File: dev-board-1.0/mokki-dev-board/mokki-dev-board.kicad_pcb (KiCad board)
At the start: 2 copper layers, 100 x 50 mm, 45 parts, among them J1 USB_B_Micro, J2 SWD connector, J3 OLED_Connector, J4 BLE_Connector, J5 DEBUG_Conn, J6 User port, Q1 BC847B, SW1 SW_PWR, SW10 BTN_B, SW2 BTN_RST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

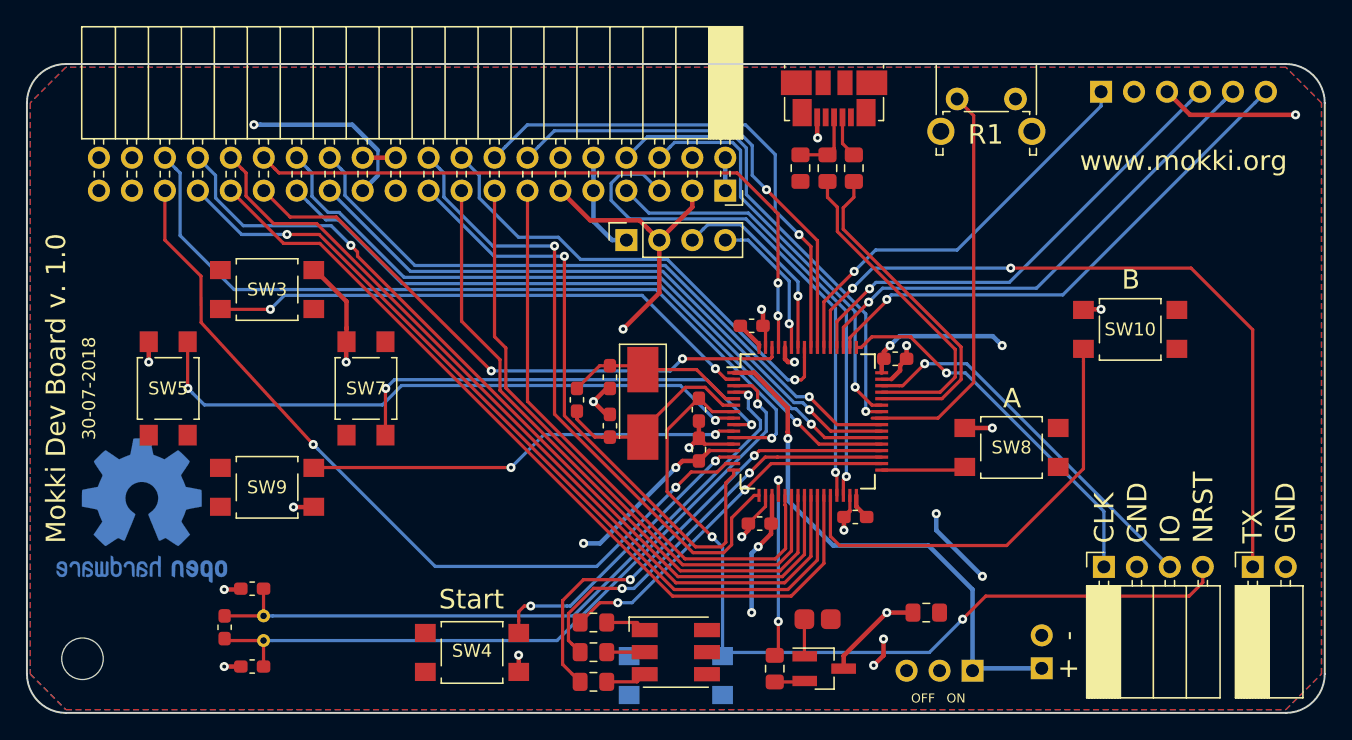
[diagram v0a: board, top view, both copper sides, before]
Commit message: Shrinked from 50mm to 45mm
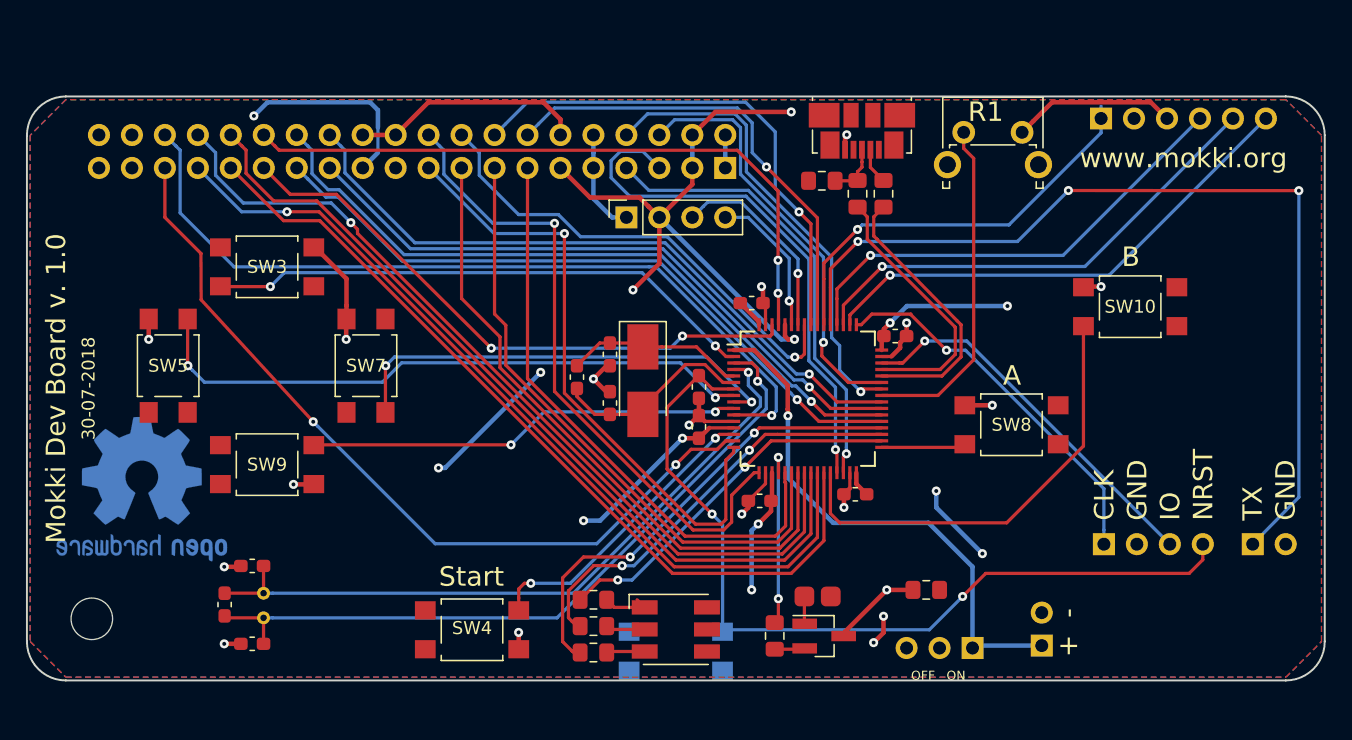
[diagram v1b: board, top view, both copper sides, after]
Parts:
- J2: footprint Connector_PinSocket_2.54mm:PinSocket_1x04_P2.54mm_Horizontal -> Connector_PinSocket_2.54mm:PinSocket_1x04_P2.54mm_Horizontal-no-drawing
- J5: footprint Connector_PinSocket_2.54mm:PinSocket_1x02_P2.54mm_Horizontal -> Connector_PinSocket_2.54mm:PinSocket_1x02_P2.54mm_Horizontal-no-drawing
- J6: footprint Connector_PinSocket_2.54mm:PinSocket_2x20_P2.54mm_Horizontal -> Connector_PinSocket_2.54mm:PinSocket_2x20_P2.54mm_Horizontal-no-drawing
- moved J1 3.30 mm to (162.8, 85.2)
- moved REF** 3.16 mm to (103.5, 122.8)
- moved R9 3.04 mm to (162.5, 90.0)
- moved R8 3.02 mm to (164.5, 90.0)
- moved SW6 2.62 mm to (170.7, 85.3)
- moved R3 2.52 mm to (156.1, 124.1)
- moved Q1 2.51 mm to (159.9, 124.1)
- moved R6 2.26 mm to (142.2, 125.3)
- moved J4 2.06 mm to (181.3, 84.2)
- moved R5 2.00 mm to (142.2, 123.3)
- moved R7 1.92 mm to (159.8, 89.0), turned to 0 degrees
- moved SW2 1.87 mm to (148.5, 125.2)
- moved BT1 1.75 mm to (176.7, 124.8)
- moved C1 1.75 mm to (143.4, 102.4)
- moved C10 1.75 mm to (150.3, 108.0)
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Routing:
- net GND: track 89.7 -> 129.7 mm
- net /USART5_TX: track 57.0 -> 71.6 mm, vias 2 -> 3
- net VCC: track 70.9 -> 83.4 mm, vias 9 -> 11
- net /GPIO_PA8: track 31.3 -> 26.1 mm
- net /USB_DM: track 26.1 -> 21.3 mm
- net /USB_DP: track 25.3 -> 20.6 mm
- net /UART4_TX: track 40.3 -> 37.5 mm
- net /GPIO_PA15: track 40.7 -> 39.1 mm
- net Net-(J1-Pad3): track 5.50 -> 4.24 mm
- net /USART1_RX: track 31.6 -> 32.7 mm
- net /UART4_RX: track 37.3 -> 36.2 mm
- net Net-(D1-Pad1): track 3.17 -> 4.00 mm
- net /DAC: track 14.8 -> 14.0 mm
- net Net-(LS1-Pad2): track 2.87 -> 2.11 mm
- net /USART1_TX: track 35.6 -> 36.2 mm
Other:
- board size 100 x 50 mm -> 100 x 45 mm

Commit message: Revert "Shrinked from 50mm to 45mm"
This reverts commit b318c16d80a30d8fc187a8b3fd500b0e07cadd18.
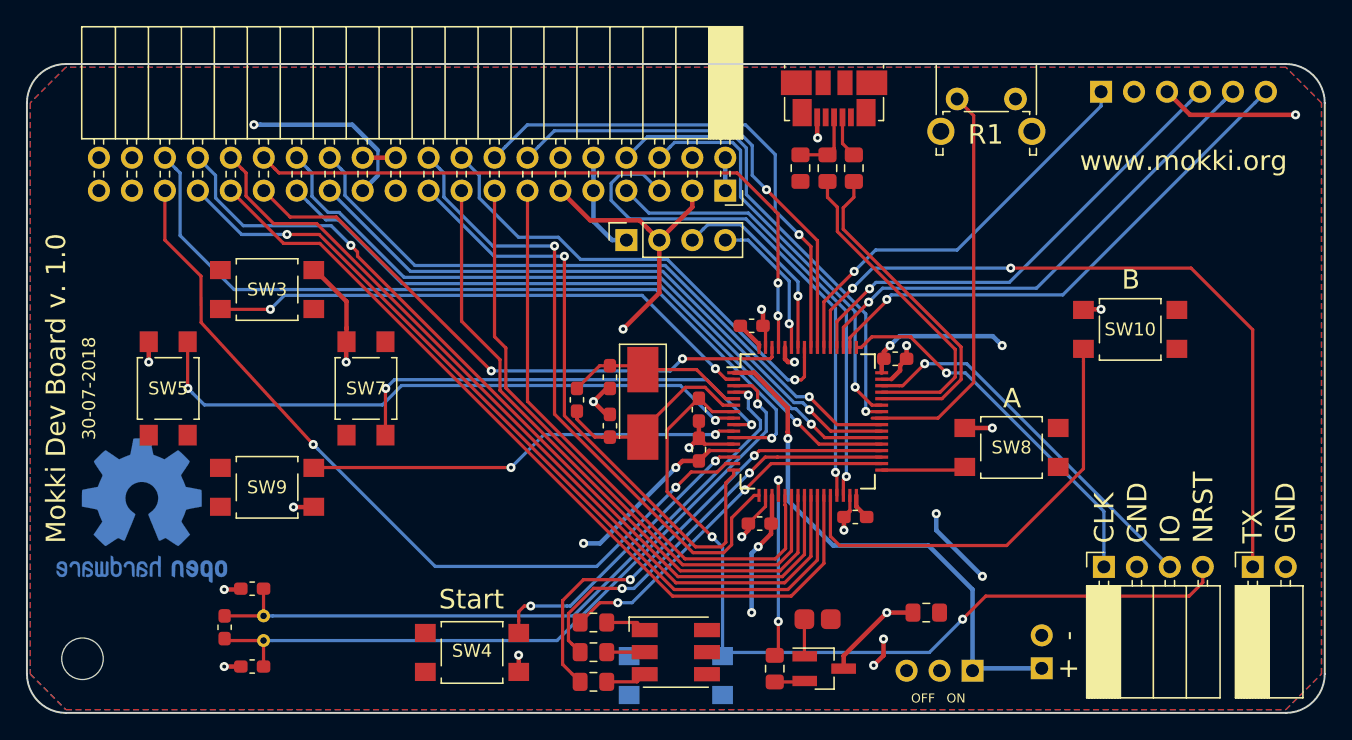
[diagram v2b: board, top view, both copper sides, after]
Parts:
- J2: footprint Connector_PinSocket_2.54mm:PinSocket_1x04_P2.54mm_Horizontal-no-drawing -> Connector_PinSocket_2.54mm:PinSocket_1x04_P2.54mm_Horizontal
- J5: footprint Connector_PinSocket_2.54mm:PinSocket_1x02_P2.54mm_Horizontal-no-drawing -> Connector_PinSocket_2.54mm:PinSocket_1x02_P2.54mm_Horizontal
- J6: footprint Connector_PinSocket_2.54mm:PinSocket_2x20_P2.54mm_Horizontal-no-drawing -> Connector_PinSocket_2.54mm:PinSocket_2x20_P2.54mm_Horizontal
- moved J1 3.30 mm to (160.7, 82.6)
- moved REF** 3.16 mm to (102.8, 125.8)
- moved R9 3.04 mm to (160.2, 88.0)
- moved R8 3.02 mm to (162.2, 88.0)
- moved SW6 2.62 mm to (170.2, 82.7)
- moved R3 2.52 mm to (156.1, 126.6)
- moved Q1 2.51 mm to (159.9, 126.6)
- moved R6 2.26 mm to (142.2, 127.6)
- moved J4 2.06 mm to (181.3, 82.1)
- moved R5 2.00 mm to (142.2, 125.3)
- moved R7 1.92 mm to (158.1, 88.0), turned to 90 degrees
- moved SW2 1.87 mm to (148.5, 127.1)
- moved BT1 1.75 mm to (176.7, 126.6)
- moved C1 1.75 mm to (143.4, 104.1)
- moved C10 1.75 mm to (150.3, 109.7)
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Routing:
- net GND: track 129.7 -> 89.7 mm
- net /USART5_TX: track 71.6 -> 57.0 mm, vias 3 -> 2
- net VCC: track 83.4 -> 70.9 mm, vias 11 -> 9
- net /GPIO_PA8: track 26.1 -> 31.3 mm
- net /USB_DM: track 21.3 -> 26.1 mm
- net /USB_DP: track 20.6 -> 25.3 mm
- net /UART4_TX: track 37.5 -> 40.3 mm
- net /GPIO_PA15: track 39.1 -> 40.7 mm
- net Net-(J1-Pad3): track 4.24 -> 5.50 mm
- net /USART1_RX: track 32.7 -> 31.6 mm
- net /UART4_RX: track 36.2 -> 37.3 mm
- net Net-(D1-Pad1): track 4.00 -> 3.17 mm
- net /DAC: track 14.0 -> 14.8 mm
- net Net-(LS1-Pad2): track 2.11 -> 2.87 mm
- net /USART1_TX: track 36.2 -> 35.6 mm
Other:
- board size 100 x 45 mm -> 100 x 50 mm

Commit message: ready to panelize
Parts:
- added R10: 100K, Resistor_SMD:R_0805_2012Metric_Pad1.15x1.40mm_HandSolder, F.Cu at (153.1, 96.6)
- J2: footprint Connector_PinSocket_2.54mm:PinSocket_1x04_P2.54mm_Horizontal -> Connector_PinSocket_2.54mm:PinSocket_1x04_P2.54mm_Horizontal-no-drawing
- J5: footprint Connector_PinSocket_2.54mm:PinSocket_1x02_P2.54mm_Horizontal -> Connector_PinSocket_2.54mm:PinSocket_1x02_P2.54mm_Horizontal-no-drawing
- J6: footprint Connector_PinSocket_2.54mm:PinSocket_2x20_P2.54mm_Horizontal -> Connector_PinSocket_2.54mm:PinSocket_2x20_P2.54mm_Vertical
- SW1: footprint Connector_PinHeader_2.54mm:PinHeader_1x03_P2.54mm_Horizontal -> Connector_PinHeader_2.54mm:PinHeader_1x03_P2.54mm_Vertical
- moved C9 2.41 mm to (166.1, 124.0)
- moved J4 1.86 mm to (181.3, 84.0)
- moved Q1 0.57 mm to (159.9, 126.0)
- moved R3 0.52 mm to (156.1, 126.1)
- moved R6 0.51 mm to (142.1, 127.1)
- moved J1 0.51 mm to (160.7, 83.2)
- moved SW6 0.46 mm to (170.2, 83.2)
- moved REF** 0.43 mm to (102.5, 125.5)
- moved R5 0.25 mm to (142.1, 125.1)
- moved SW2 0.12 mm to (148.5, 127.0)
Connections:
- U1 pad 60: GND -> Net-(R10-Pad1)
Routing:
- net GND: track 89.7 -> 76.7 mm, vias 21 -> 17
- net Net-(R10-Pad1): track 0.00 -> 9.16 mm, vias 0 -> 2
- net VCC: track 70.9 -> 63.8 mm, vias 9 -> 7
- net /USART5_TX: track 57.0 -> 52.5 mm, vias 2 -> 3
- net /UART4_TX: track 40.3 -> 37.9 mm
- net /UART4_RX: track 37.3 -> 36.0 mm
- net /GPIO_PB15: track 36.2 -> 34.9 mm
- net /GPIO_PA15: track 40.7 -> 39.9 mm
- net /GPIO_PD2: track 32.2 -> 31.4 mm
- net Net-(LS1-Pad2): track 2.87 -> 2.30 mm
- net /NRST: track 65.9 -> 66.5 mm, vias 2 -> 4
- net /GPIO_PB8_T: vias 2 -> 0
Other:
- board size 100 x 50 mm -> 100 x 49 mm
- board text added: "1"
- board text added: "1-08-2018"
- board text added: "10"
- board text added: "11"
- board text added: "12"
- board text added: "2"
- board text added: "3"
- board text added: "4"
- board text added: "5"
- board text added: "6"
- board text added: "7"
- board text added: "8"
- board text added: "9"
- board text added: "I2C2 SCL"
- board text added: "I2C2 SDA"
- board text added: "SPI1 CLK"
- board text added: "SPI1 MISO"
- board text added: "SPI1 MOSI"
- board text added: "SPI3 CLK"
- board text added: "SPI3 MISO"
- board text added: "SPI3 MOSI"
- board text added: "UART1 RX"
- board text added: "UART1 TX"
- board text added: "UART2 RX"
- board text added: "UART2 TX"
- board text added: "VCC"
- board text removed: "30-07-2018"
